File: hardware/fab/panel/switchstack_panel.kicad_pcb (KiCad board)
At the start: 4 copper layers, 173.4 x 64.4 mm, 239 parts

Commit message: Nutzen bestueckfaehig, Masse-Bruecken, Klinken-Ausnahme
NUTZEN. Er hatte weder Passermarken noch Werkzeugbohrungen und nur 4 mm
Rand - so nimmt ihn kein Bestuecker an. Jetzt:

  drei Passermarken  Kupferpunkt 1,0 mit 3,0 Freistellung, bewusst NICHT
                     drehsymmetrisch angeordnet - verdreht eingelegt passt
                     das Muster nicht mehr
  zwei Werkzeugbohrungen  3,0 mm NPTH in den breiten Raendern
  Rand oben/unten    4 -> 8 mm; dort klemmen die Automaten, ueblich sind
                     mindestens 5 mm

Der Nutzen waechst dadurch von 173,4 x 64,4 auf 173,4 x 72,4 mm, also von
112 auf 126 cm2.

MASSE-BRUECKEN. gnd_connect setzte bisher nur Stitching-Vias, und die
brauchen Eigenkupfer UEBER einem Flaechenfragment der Gegenlage. Fast alle
Reste erfuellen das nicht. Neu sucht das Skript radial nach einer freien
geraden Verbindung auf derselben Lage - bis 6 mm, 0,4 mm breit, und nur
dort, wo seg_clear die ganze Strecke freigibt.

Ziel ist dabei NICHT der Hauptcluster, sondern irgendein anderer: Die Runden
wiederholen sich, und was einmal verbunden ist, waechst zusammen. Nur auf den
Hauptcluster zu zielen liess fast alles stehen, weil die naechste Flaeche
meist einem anderen Rest gehoerte.

Zwei Sicherungen: Bruecken duerfen nicht ausserhalb der Platine beginnen -
das Massepad der Klinkenbuchse ragt absichtlich ueber die Kante, und eine
Bahn von dort erzeugte prompt einen zweiten Randabstandsfehler.

  Masse-Inseln Bottom  26 -> 24

KLINKENBUCHSE. Ihr Ueberhang ueber die Boardkante ist beabsichtigt und wird
von gen_layouts auch so gemeldet, erzeugte in der DRC aber dauerhaft einen
Randabstandsfehler und verdeckte damit echte Funde. Eigene Regel, die NUR
fuer J6 auf dem Top-Board gilt - auf Mid heisst J6 der Haubenkontakt und darf
nicht ueberstehen.

  top_ui hat damit NULL Kupferfehler.

NICHT GELUNGEN: Der Haarriss auf Bottom (0,1465 statt 0,15 mm, ein Fehlbetrag
von 3,5 Mikrometern) laesst sich nicht durch Verschmaelern des 0,18-mm-Stuecks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
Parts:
- added FID: , , F.Cu at (-82.7, -32.2)
- added FID: , , F.Cu at (-82.7, 32.2)
- added FID: , , F.Cu at (82.7, -32.2)
- added TOOL: , , F.Cu at (-76.7, 32.2)
- added TOOL: , , F.Cu at (76.7, 32.2)
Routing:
- net BOT_PGND: track 0.00 -> 23.0 mm
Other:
- board size 173.4 x 64.4 mm -> 173.4 x 72.4 mm

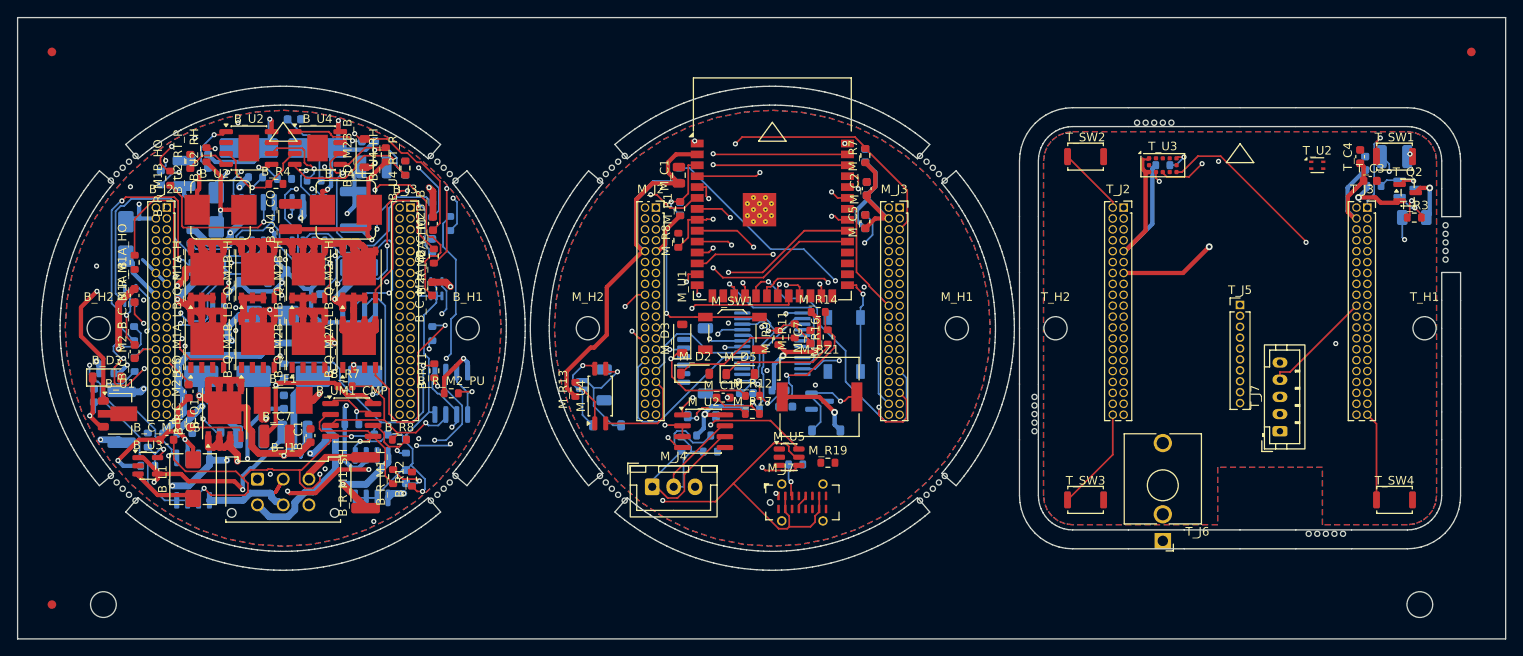
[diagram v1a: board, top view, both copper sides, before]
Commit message: Der Original-Controller bestaetigt die Strommessung ein viertes Mal
Der mitgelieferte K0000230 lag offen auf dem Tisch. Drei Bauteile darauf
sagen dasselbe wie unsere drei Messungen - und man muss dafuer nichts messen:

  Shunt 50 mOhm je Kanal   bei 1,7 A sind das 85 mV und 0,14 W.
                           Bei 20 A waeren es 20 WATT in einem Chipwiderstand.
  2x Infineon BTM7700G     integrierte H-Bruecke, rund 110 mOhm im Strompfad.
                           Bei 1,7 A 0,32 W, bei 20 A 44 W in einem SO-28.
  Elko 47 uF               fuer zwei Motoren. Wer 20-A-Impulse abfaengt,
                           baut Hunderte von Mikrofarad ein.

Drei unabhaengige Bauteilentscheidungen, alle nur mit ein bis zwei Ampere
vereinbar. docs/14 neu, mit der vollstaendigen Bauteilliste.

DREI FOLGERUNGEN FUER UNS

1) Unsere diskrete Bruecke aus acht MOSFETs und vier Gate-Treibern loest der
   Hersteller mit ZWEI ICs. Das war Punkt 55; das Argument dagegen (Platine
   ist geroutet) steht weiter, aber die Sachlage ist jetzt belegt statt
   vermutet. Der BTM7700G selbst waere fuer uns grenzwertig - seine
   Kurzschlussfestigkeit endet bei 28 V, unsere Schiene liegt bei 26,4 V.

2) Der Bulk-Kondensator darf schrumpfen. docs/01 sieht 470 bis 1000 uF vor,
   das Original kommt mit 47 uF aus. Das ist die praktisch wertvollste
   Erkenntnis, denn der Elko ist eines der groessten Teile auf der Kabelseite
   von Bottom - genau dort, wo heute der Platz fuer einen zusammengefassten
   Feldstecker fehlt. Nicht blind uebernehmen: 100 bis 220 uF sind die
   naheliegende Groessenordnung fuer unsere PWM-Topologie.

3) Der Hersteller trennt seine Eingaenge galvanisch (zwei Optokoppler), wir
   nicht. Bei reiner SELV-Verkabelung zulaessig, aber ein Konzeptunterschied.

Ausserdem in diesem Commit:

  3D-Modelle fuer die drei Steckverbinder, die KiCad nicht mitliefert
  (mechanical/connector_models.py) - Huellkoerper aus dem F.Fab-Grundriss,
  Hoehen mit Quelle dokumentiert. gen_layouts haengt sie 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
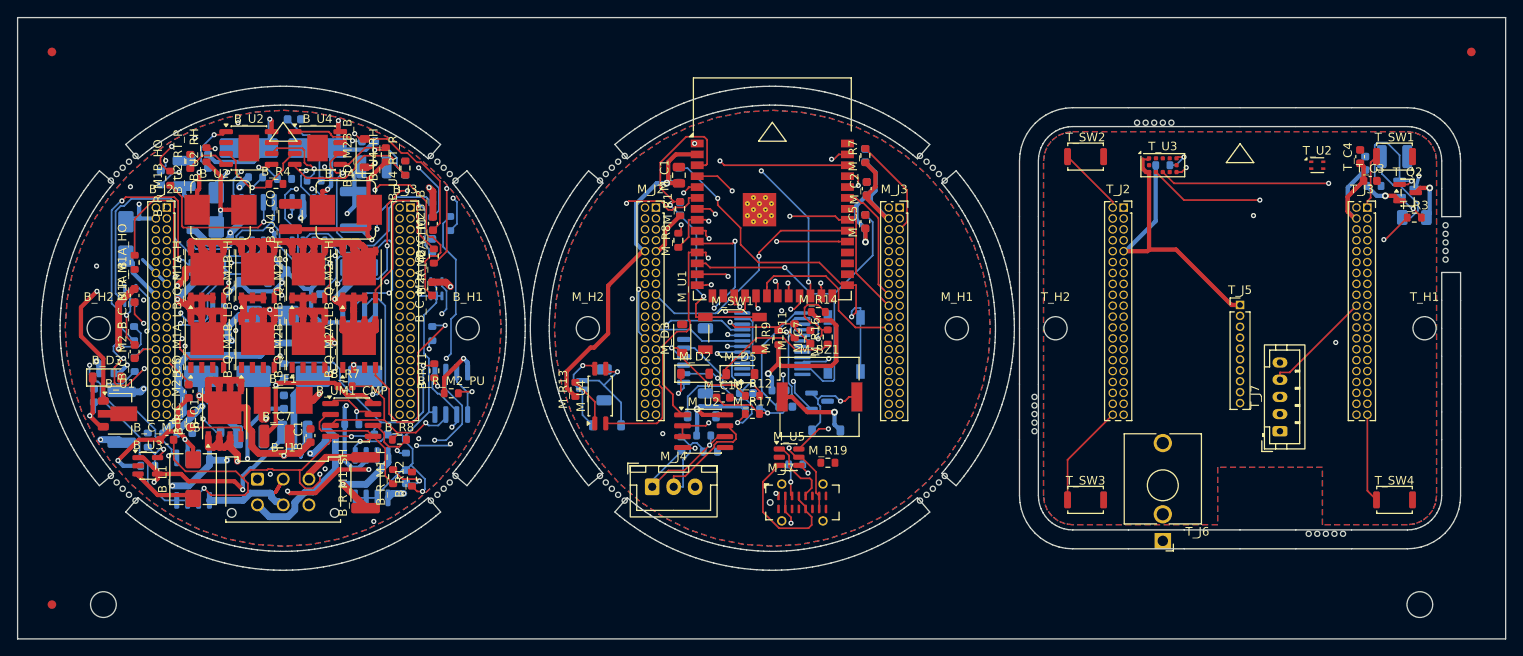
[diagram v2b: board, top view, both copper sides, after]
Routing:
- net MID_M2_INB: track 0.00 -> 47.1 mm, vias 0 -> 3
- net MID_AUDIO_B: track 0.00 -> 30.0 mm, vias 0 -> 2
- net MID_QSPI_D2: track 39.7 -> 18.1 mm, vias 3 -> 1
- net MID_REED1_IN: track 15.0 -> 36.1 mm, vias 0 -> 3
- net MID_USB_DP_C: track 0.00 -> 16.9 mm
- net MID_3V3_SYS: track 177.2 -> 166.5 mm, vias 2 -> 4
- net MID_RS485_A: track 26.6 -> 17.6 mm, vias 0 -> 1
- net TOP_STAR_G: track 5.92 -> 14.6 mm
- net MID_ESP_EN: track 31.8 -> 39.8 mm
- net MID_USB_VBUS: track 66.0 -> 58.3 mm
- net MID_SAB1_IN: track 13.5 -> 20.2 mm, vias 0 -> 1
- net MID_USB_DN_C: track 1.85 -> 8.17 mm
- net MID_I2C_SDA: track 63.9 -> 69.8 mm, vias 3 -> 1
- net TOP_STAR_EN: track 50.5 -> 44.8 mm, vias 2 -> 1
- net MID_AUDIO_PWM: track 54.2 -> 48.5 mm
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
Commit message: Endstand nach dem Umbau: 13 offene Signale, 23 Masse-Inseln, ein Haarriss
Alle drei Boards mit der integrierten Bruecke, dem gemeinsamen Feldstecker,
der quergestellten USB-Buchse und den zusammengelegten Frontsensoren neu
erzeugt und geroutet.

              Bauteile  Segmente  offene Signale  Masse-Inseln  Kupferfehler
  top_ui         20        149          3               1            0
  mid_logic      47        795          3              12            1
  bottom         79        768          7              10            0

Bottom hat 23 Bauteile weniger als vorher und zum ersten Mal null
Kupferfehler. Auf Top haengen alle drei offenen Netze am selben Bauteil - dem
Raumsensor, der gerade neben den ToF gewandert ist; der Router kam zwischen
ihm und dem Ecktaster nicht mehr heraus.

MITERZEUGT: Nutzen (173,4 x 72,4 mm, deckungsgleich mit der Summe der
Einzelboards), Bestellunterlagen fuer alle vier, 3D-Renderings und die
STEP-Baugruppe. Die misst jetzt 70 x 72,3 x 39,6 mm - sie ist gewachsen, weil
die Klinkenbuchse mittig sitzt und ihr Modell nach hinten ragt.

Die Stueckliste ist von 46 auf 42 Positionen geschrumpft (Bottom) bzw. von 28
auf 25 (Mid). Ohne LCSC-Nummer sind weiterhin alle - das bleibt der naechste
Schritt vor der Bestellung.

docs/13 und docs/16 auf die Endzahlen.

Co-Authored-By: Claude Opus 5 (1M context) <noreply@anthropic.com>
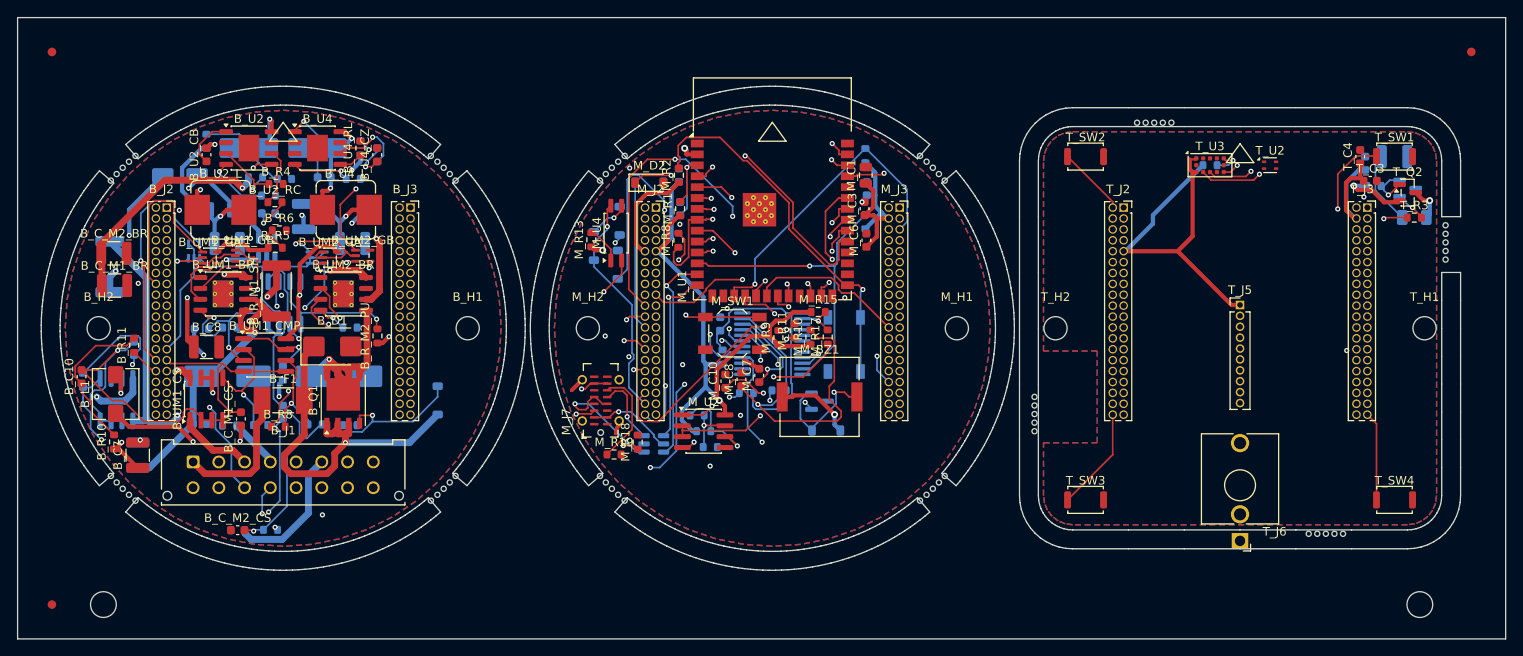
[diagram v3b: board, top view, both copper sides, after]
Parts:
- removed B_C5, B_C6: 1u, C_0603_1608Metric
- removed B_C_M1A_B, B_C_M1B_B, B_C_M2A_B, B_C_M2B_B: 100n, C_0603_1608Metric
- removed B_D3: 27V, D_SOD-123
- removed B_D_M1A_B, B_D_M1B_B, B_D_M2A_B, B_D_M2B_B: 100V 1A, D_SOD-123
- removed B_Q_M1A_H, B_Q_M1A_L, B_Q_M1B_H, B_Q_M1B_L, B_Q_M2A_H, B_Q_M2A_L, B_Q_M2B_H, B_Q_M2B_L: N-FET 40V 60A, PowerPAK_SO-8_Single
- removed B_R2: 100R, R_0603_1608Metric
- removed B_R_M1A_HO, B_R_M1A_LO, B_R_M1B_HO, B_R_M1B_LO, B_R_M2A_HO, B_R_M2A_LO, B_R_M2B_HO, B_R_M2B_LO: 10R, R_0603_1608Metric
- removed B_U1: L78L12, SOT-89-3
- removed B_UM1A_DRV, B_UM1B_DRV, B_UM2A_DRV, B_UM2B_DRV: IR2104, SOIC-8_3.9x4.9mm_P1.27mm
- removed M_J4: RS485 A/B/GND, JST_XH_B3B-XH-A_1x03_P2.50mm_Vertical
- removed M_J5: Feld: 4 Reed, JST_SH_BM06B-SRSS-TB_1x06-1MP_P1.00mm_Vertical
- removed M_J6: Haubenkontakt, JST_SH_BM02B-SRSS-TB_1x02-1MP_P1.00mm_Vertical
- removed T_J7: Reserve UART, JST_PH_B5B-PH-K_1x05_P2.00mm_Vertical
- added B_C_M1_BR: 100u 50V, C_1210_3225Metric, F.Cu at (-75.4, -4.97)
- added B_C_M2_BR: 100u 50V, C_1210_3225Metric, F.Cu at (-75.5, -8.73)
- added B_R_M1_IL: 33k0, R_0603_1608Metric, B.Cu at (-62.0, -0.08)
- added B_R_M2_IL: 33k0, R_0603_1608Metric, B.Cu at (-48.0, -0.08)
- added B_UM1_BR: DRV8871, HSOP-8-1EP_3.9x4.9mm_P1.27mm_EP2.41x3.1mm_ThermalVias, F.Cu at (-62.8, -4.00)
- added B_UM1_GA: 74AHC1G08, SOT-353_SC-70-5, F.Cu at (-64.3, -8.23)
- added B_UM1_GB: 74AHC1G08, SOT-353_SC-70-5, F.Cu at (-60.5, -8.46)
- added B_UM2_BR: DRV8871, HSOP-8-1EP_3.9x4.9mm_P1.27mm_EP2.41x3.1mm_ThermalVias, F.Cu at (-48.8, -4.00)
- added B_UM2_GA: 74AHC1G08, SOT-353_SC-70-5, F.Cu at (-50.3, -8.23)
- added B_UM2_GB: 74AHC1G08, SOT-353_SC-70-5, F.Cu at (-46.5, -8.46)
- B_C1, B_C_M2_F, B_R1, B_R12, B_R7, B_R_M1_F, B_U2_RH, B_U2_RT_R, B_U3, B_U4_CO, B_U4_RH, B_U4_RT_R, M_C2, M_C5, M_D3, M_D5, M_R12, M_R14, M_R16, M_R7, M_U5: moved to B.Cu
- B_C10, B_C8, B_D1, B_R10, B_R5, B_R6, B_U2_CB, B_U2_RC, B_U4_CZ, B_U4_RL, B_UM1_CS, M_C3, M_C6, M_C8, M_R10, M_R15, M_R18, M_R2: moved to F.Cu
- B_J1: value Power/Motor 6p -> Feld 16p; footprint Molex_Micro-Fit_3.0_43045-0612_2x03_P3.00mm_Vertical -> Molex_Micro-Fit_3.0_43045-1612_2x08_P3.00mm_Vertical
- moved B_C10 35.5 mm to (-79.2, 5.64), turned to 90 degrees
- moved B_R11 35.1 mm to (-73.1, 1.99)
- moved B_R5 29.4 mm to (-56.7, -9.38)
- moved B_U3 28.9 mm to (-57.7, -9.38), turned to 90 degrees
- moved B_R6 28.8 mm to (-56.2, -11.4), turned to 0 degrees
- moved B_D2 27.2 mm to (-37.8, 8.40), turned to 90 degrees
- moved M_J7 26.3 mm to (-18.8, 8.40), turned to 90 degrees
- moved M_R19 24.9 mm to (-17.2, 14.7)
- moved B_R_M1_SH 24.6 mm to (-56.5, -4.34)
- moved M_D2 22.9 mm to (-13.1, -17.0)
- moved M_D5 22.7 mm to (-16.5, -12.5), turned to 90 degrees
- moved M_C5 22.4 mm to (-9.64, -17.8)
- moved B_UM2_CMP 22.1 mm to (-55.6, -2.96)
- moved M_C1 21.8 mm to (12.1, -17.8)
- moved B_R10 21.5 mm to (-75.5, 13.2)
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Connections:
- net TOP_RSV_A2 renamed TOP_REED2_IN
- net TOP_RSV_A3 renamed TOP_RS485_A
- net TOP_RSV_A4 renamed TOP_RS485_B
- net TOP_RSV_A5 renamed TOP_REED1_IN
- net TOP_RSV_A6 renamed TOP_SAB1_IN
- B_J2 pad 24: BOT_RSV_A2 -> BOT_REED2_IN
- B_J2 pad 25: BOT_PGND -> BOT_SAB2_IN
- B_J2 pad 34: BOT_RSV_A3 -> BOT_RS485_A
- B_J2 pad 35: BOT_RSV_A4 -> BOT_RS485_B
- B_J2 pad 36: BOT_RSV_A5 -> BOT_REED1_IN
- B_J2 pad 37: BOT_RSV_A6 -> BOT_SAB1_IN
- B_J2 pad 38: BOT_PGND -> BOT_HOOD_A
- B_J2 pad 39: BOT_PGND -> BOT_HOOD_B
- M_J2 pad 24: MID_RSV_A2 -> MID_REED2_IN
- M_J2 pad 25: MID_PGND -> MID_SAB2_IN
- M_J2 pad 34: MID_RSV_A3 -> MID_RS485_A
- M_J2 pad 35: MID_RSV_A4 -> MID_RS485_B
- M_J2 pad 36: MID_RSV_A5 -> MID_REED1_IN
- M_J2 pad 37: MID_RSV_A6 -> MID_SAB1_IN
- M_J2 pad 38: MID_PGND -> MID_HOOD_A
- M_J2 pad 39: MID_PGND -> MID_HOOD_B
- T_J2 pad 25: TOP_PGND -> TOP_SAB2_IN
- T_J2 pad 38: TOP_PGND -> TOP_HOOD_A
- T_J2 pad 39: TOP_PGND -> TOP_HOOD_B
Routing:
- net BOT_12V_GATE: track 175.8 -> 0.00 mm, vias 13 -> 0
- net BOT_M1_SWA: track 113.7 -> 19.4 mm, vias 3 -> 2
- net BOT_M2_SWB: track 85.6 -> 0.00 mm, vias 3 -> 0
- net BOT_M2_INA: track 124.0 -> 39.2 mm, vias 5 -> 3
- net BOT_24V_PROT: track 165.3 -> 104.2 mm, vias 5 -> 3
- net BOT_M1_SWB: track 58.6 -> 0.00 mm, vias 3 -> 0
- net BOT_TRIP_RST: track 59.4 -> 3.44 mm, vias 1 -> 0
- net BOT_M1A_VB: track 49.0 -> 0.00 mm, vias 3 -> 0
- net BOT_5V_SYS: track 86.5 -> 37.6 mm, vias 5 -> 2
- net BOT_M2_SD: track 58.4 -> 12.9 mm, vias 2 -> 1
- net BOT_M1A_LO_GT: track 42.5 -> 0.00 mm, vias 3 -> 0
- net BOT_M2A_LO_G: track 42.4 -> 0.00 mm, vias 2 -> 0
- net BOT_M2B_LO_GT: track 40.8 -> 0.00 mm, vias 2 -> 0
- net BOT_M2A_VB: track 40.7 -> 0.00 mm, vias 2 -> 0
- net MID_RELAY_CTL: track 28.0 -> 67.6 mm, vias 1 -> 4
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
